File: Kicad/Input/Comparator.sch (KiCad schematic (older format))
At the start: 6 parts

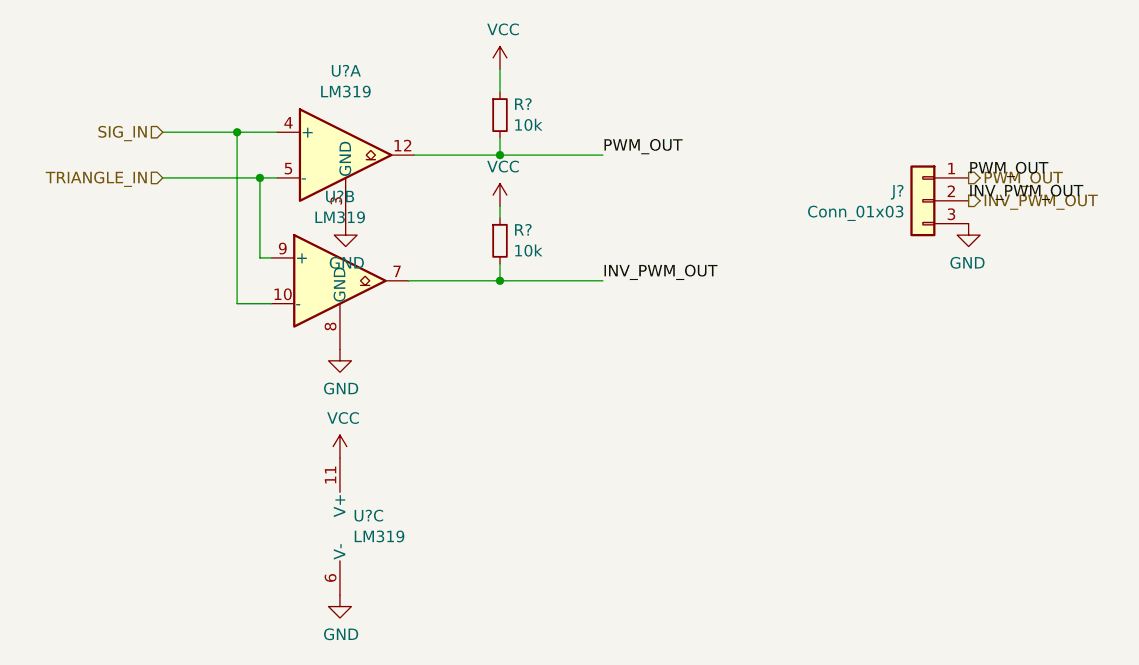
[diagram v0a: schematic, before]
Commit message: Input PCB added
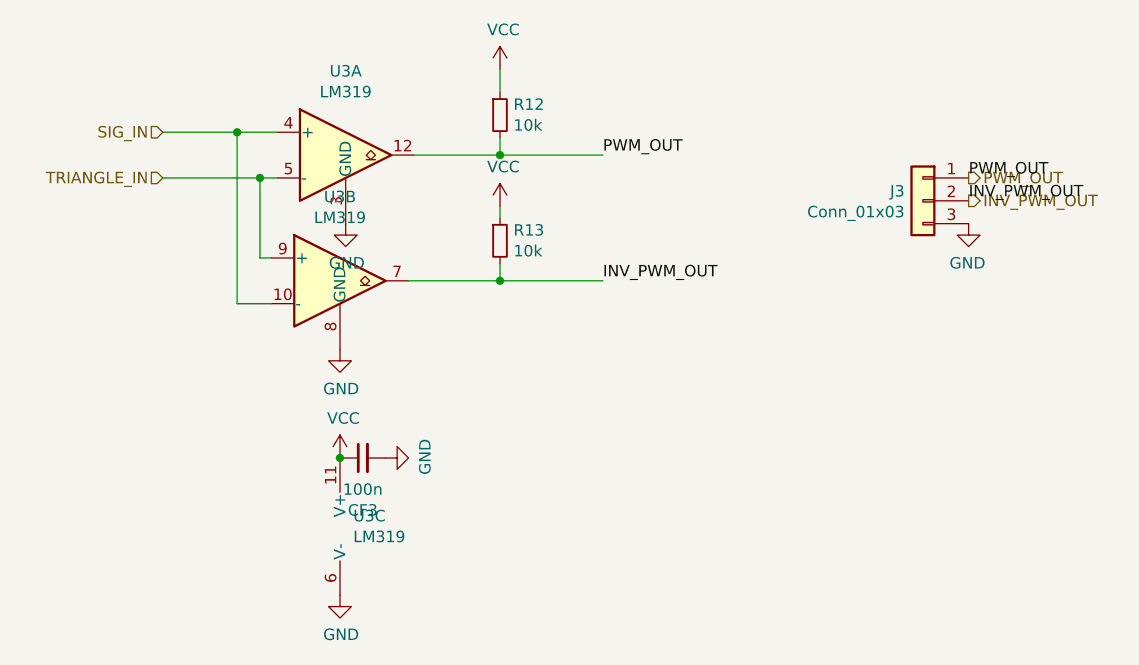
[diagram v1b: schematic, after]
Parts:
- added CF3: 100n, Capacitor_SMD:C_0603_1608Metric_Pad1.08x0.95mm_HandSolder, symbol Device:C_Small
- gave numbers to parts that had none: 4
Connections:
- net GND: now also CF3.2
- net VCC: now also CF3.1
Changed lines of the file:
@@
 $Descr A4 11693 8268
 encoding utf-8
-Sheet 3 4
+Sheet 4 4
 Title ""
 Date ""
@@
 $EndDescr
 $Comp
-L Comparator:LM319 U?
+L Comparator:LM319 U3
 U 1 1 61116116
 P 5150 2875
-F 0 "U?" H 5150 3242 50  0000 C CNN
+F 0 "U3" H 5150 3242 50  0000 C CNN
 F 1 "LM319" H 5150 3151 50  0000 C CNN
 F 2 "Package_SO:SO-14_3.9x8.65mm_P1.27mm" H 5150 2875 50  0001 C CNN
@@
 $EndComp
 $Comp
-L Comparator:LM319 U?
+L Comparator:LM319 U3
 U 2 1 6111611C
 P 5125 3425
-F 0 "U?" H 5125 3792 50  0000 C CNN
+F 0 "U3" H 5125 3792 50  0000 C CNN
 F 1 "LM319" H 5125 3701 50  0000 C CNN
 F 2 "Package_SO:SO-14_3.9x8.65mm_P1.27mm" H 5125 3425 50  0001 C CNN
@@
 $EndComp
 $Comp
-L Comparator:LM319 U?
+L Comparator:LM319 U3
 U 3 1 61116122
 P 5225 4500
-F 0 "U?" H 5183 4546 50  0000 L CNN
+F 0 "U3" H 5183 4546 50  0000 L CNN
 F 1 "LM319" H 5183 4455 50  0000 L CNN
 F 2 "Package_SO:SO-14_3.9x8.65mm_P1.27mm" H 5225 4500 50  0001 C CNN
@@
 	4675 3525 4825 3525
 $Comp
-L power:GND #PWR?
+L power:GND #PWR0112
 U 1 1 61116132
 P 5150 3175
-F 0 "#PWR?" H 5150 2925 50  0001 C CNN
+F 0 "#PWR0112" H 5150 2925 50  0001 C CNN
 F 1 "GND" H 5155 3002 50  0000 C CNN
 F 2 "" H 5150 3175 50  0001 C CNN
@@
 $EndComp
 $Comp
-L power:GND #PWR?
+L power:GND #PWR0113
 U 1 1 61116138
 P 5125 3725
-F 0 "#PWR?" H 5125 3475 50  0001 C CNN
+F 0 "#PWR0113" H 5125 3475 50  0001 C CNN
 F 1 "GND" H 5130 3552 50  0000 C CNN
 F 2 "" H 5125 3725 50  0001 C CNN
@@
 $EndComp
 $Comp
-L power:GND #PWR?
+L power:GND #PWR0114
 U 1 1 6111613E
 P 5125 4800
-F 0 "#PWR?" H 5125 4550 50  0001 C CNN
+F 0 "#PWR0114" H 5125 4550 50  0001 C CNN
 F 1 "GND" H 5130 4627 50  0000 C CNN
 F 2 "" H 5125 4800 50  0001 C CNN
@@
 $EndComp
 $Comp
-L power:VCC #PWR?
+L power:VCC #PWR0115
 U 1 1 61116144
 P 5125 4200
-F 0 "#PWR?" H 5125 4050 50  0001 C CNN
+F 0 "#PWR0115" H 5125 4050 50  0001 C CNN
 F 1 "VCC" H 5140 4373 50  0000 C CNN
 F 2 "" H 5125 4200 50  0001 C CNN
@@
 	5425 3425 5825 3425
 $Comp
-L Device:R_Small R?
+L Device:R_Small R12
 U 1 1 61119BD5
 P 5825 2700
-F 0 "R?" H 5884 2746 50  0000 L CNN
+F 0 "R12" H 5884 2746 50  0000 L CNN
 F 1 "10k" H 5884 2655 50  0000 L CNN
 F 2 "Resistor_SMD:R_0603_1608Metric_Pad0.98x0.95mm_HandSolder" H 5825 2700 50  0001 C CNN
@@
 $EndComp
 $Comp
-L Device:R_Small R?
+L Device:R_Small R13
 U 1 1 6111A188
 P 5825 3250
-F 0 "R?" H 5884 3296 50  0000 L CNN
+F 0 "R13" H 5884 3296 50  0000 L CNN
 F 1 "10k" H 5884 3205 50  0000 L CNN
 F 2 "Resistor_SMD:R_0603_1608Metric_Pad0.98x0.95mm_HandSolder" H 5825 3250 50  0001 C CNN
@@
 $EndComp
 $Comp
-L power:VCC #PWR?
+L power:VCC #PWR0116
 U 1 1 6111A8CA
 P 5825 2500
-F 0 "#PWR?" H 5825 2350 50  0001 C CNN
+F 0 "#PWR0116" H 5825 2350 50  0001 C CNN
 F 1 "VCC" H 5840 2673 50  0000 C CNN
 F 2 "" H 5825 2500 50  0001 C CNN
@@
 $EndComp
 $Comp
-L power:VCC #PWR?
+L power:VCC #PWR0117
 U 1 1 6111AE94
 P 5825 3100
-F 0 "#PWR?" H 5825 2950 50  0001 C CNN
+F 0 "#PWR0117" H 5825 2950 50  0001 C CNN
 F 1 "VCC" H 5840 3273 50  0000 C CNN
 F 2 "" H 5825 3100 50  0001 C CNN
@@
 Connection ~ 4775 2975
 $Comp
-L Connector_Generic:Conn_01x03 J?
+L Connector_Generic:Conn_01x03 J3
 U 1 1 611080B2
 P 7675 3075
-F 0 "J?" H 7755 3117 50  0000 L CNN
+F 0 "J3" H 7755 3117 50  0000 L CNN
 F 1 "Conn_01x03" H 7755 3026 50  0000 L CNN
 F 2 "TerminalBlock:TerminalBlock_bornier-3_P5.08mm" H 7675 3075 50  0001 C CNN
@@
 	6275 2875 5825 2875
 $Comp
-L power:GND #PWR?
+L power:GND #PWR0118
 U 1 1 6110885B
 P 7875 3175
-F 0 "#PWR?" H 7875 2925 50  0001 C CNN
+F 0 "#PWR0118" H 7875 2925 50  0001 C CNN
 F 1 "GND" H 7880 3002 50  0000 C CNN
 F 2 "" H 7875 3175 50  0001 C CNN
@@
 Text Label 6275 3425 0    50   ~ 0
 INV_PWM_OUT
+$Comp
+L Device:C_Small CF?
+U 1 1 61173FA6
+P 5225 4200
+AR Path="/610C616D/61173FA6" Ref="CF?"  Part="1"
+AR Path="/611D4178/61173FA6" Ref="CF?"  Part="1"
+AR Path="/6113023B/61173FA6" Ref="CF?"  Part="1"
+AR Path="/61130364/61173FA6" Ref="CF3"  Part="1"
+F 0 "CF3" V 4996 4200 50  0000 C CNN
+F 1 "100n" V 5087 4200 50  0000 C CNN
+F 2 "Capacitor_SMD:C_0603_1608Metric_Pad1.08x0.95mm_HandSolder" H 5225 4200 50  0001 C CNN
+F 3 "~" H 5225 4200 50  0001 C CNN
+	1    5225 4200
+	0    -1   -1   0
+$EndComp
+$Comp
+L power:GND #PWR?
+U 1 1 61173FAC
+P 5325 4200
+AR Path="/6113023B/61173FAC" Ref="#PWR?"  Part="1"
+AR Path="/61130364/61173FAC" Ref="#PWR0121"  Part="1"
+F 0 "#PWR0121" H 5325 3950 50  0001 C CNN
+F 1 "GND" H 5330 4027 50  0000 C CNN
+F 2 "" H 5325 4200 50  0001 C CNN
+F 3 "" H 5325 4200 50  0001 C CNN
+	1    5325 4200
+	0    -1   -1   0
+$EndComp
+Connection ~ 5125 4200
 $EndSCHEMATC
